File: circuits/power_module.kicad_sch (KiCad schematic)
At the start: 0 parts

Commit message: added 5V reg circuit
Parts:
- added C1: 10uF, symbol Device:C_Small
- added C2, C3: 0.1uF, symbol Device:C_Small
- added C4, C5: 22uF, symbol Device:C_Small
- added C6: 75pF, symbol Device:C_Small
- added J1: Conn_01x02_Pin, symbol Connector:Conn_01x02_Pin
- added L1: 15uH, symbol Device:L_Small
- added R1: 511k, symbol Device:R_Small
- added R2: 105k, symbol Device:R_Small
- added R3: 49.9, symbol Device:R_Small
- added R4: 100k, symbol Device:R_Small
- added R5: 13.3k, symbol Device:R_Small
- added U1: TPS54202DDC, Package_TO_SOT_SMD:SOT-23-6, symbol Regulator_Switching:TPS54202DDC
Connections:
- new net: R1.2, R2.1, U1.5 (EN)
- new net: C6.2, R4.2, R5.1, U1.4 (FB)
- new net: C6.1, R3.2, R4.1
- new net: C3.1, U1.6 (BOOT)
- new net: C3.2, L1.1, U1.2 (SW)
- new net +5V: C4.1, C5.1, L1.2, R3.1
- new net +BATT: C1.1, C2.1, J1.1 (Pin_1), R1.1, U1.3 (VIN)
- new net GND: C1.2, C2.2, C4.2, C5.2, J1.2 (Pin_2), R2.2, R5.2, U1.1 (GND)
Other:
- note added: "5V regulator"

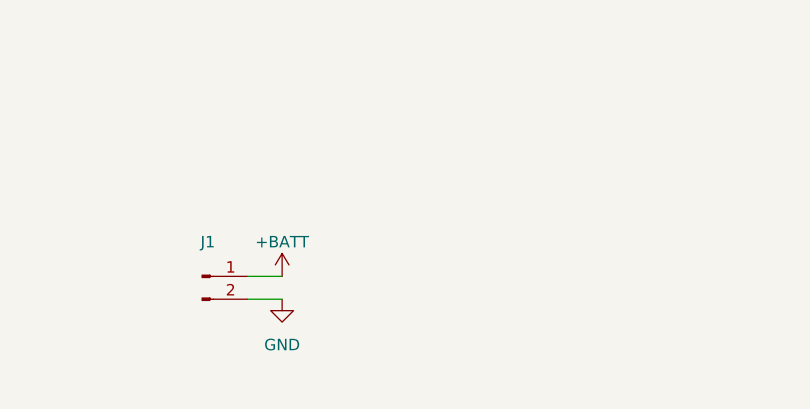
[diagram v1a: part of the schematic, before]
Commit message: motor shield circuit
BTN7030-1EPA
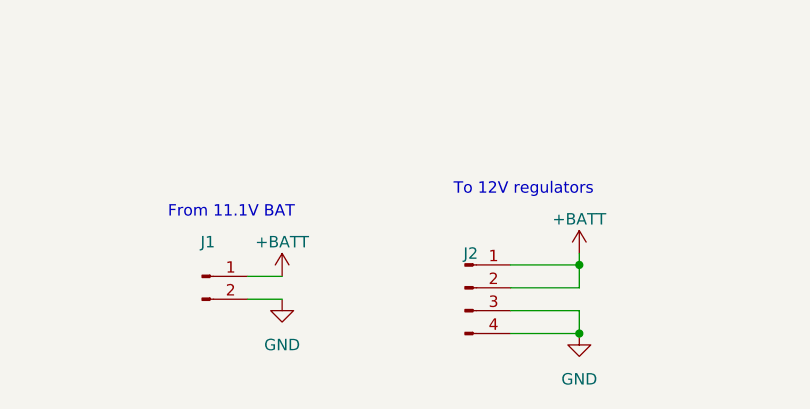
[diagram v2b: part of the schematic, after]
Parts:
- added J2: Conn_01x04_Pin, symbol Connector:Conn_01x04_Pin
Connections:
- net +BATT: now also J2.1 (Pin_1), J2.2 (Pin_2)
- net GND: now also J2.3 (Pin_3), J2.4 (Pin_4)
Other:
- note added: "From 11.1V BAT"
- note added: "To 12V regulators"
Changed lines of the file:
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@@
   (junction (at 105.41 62.23) (diameter 0) (color 0 0 0 0)
   )
+  (junction (at 101.6 185.42) (diameter 0) (color 0 0 0 0)
+  )
   (junction (at 44.45 53.34) (diameter 0) (color 0 0 0 0)
   )
@@
   (junction (at 105.41 55.88) (diameter 0) (color 0 0 0 0)
   )
+  (junction (at 101.6 177.8) (diameter 0) (color 0 0 0 0)
+  )
   (junction (at 119.38 71.12) (diameter 0) (color 0 0 0 0)
   )
@@
     (stroke (width 0) (type default))
   )
+  (wire (pts (xy 93.98 177.8) (xy 101.6 177.8))
+    (stroke (width 0) (type default))
+  )
   (wire (pts (xy 54.61 58.42) (xy 54.61 59.69))
     (stroke (width 0) (type default))
@@
     (stroke (width 0) (type default))
   )
+  (wire (pts (xy 93.98 185.42) (xy 101.6 185.42))
+    (stroke (width 0) (type default))
+  )
   (wire (pts (xy 38.1 50.8) (xy 38.1 53.34))
     (stroke (width 0) (type default))
@@
     (stroke (width 0) (type default))
   )
+  (wire (pts (xy 101.6 182.88) (xy 101.6 185.42))
+    (stroke (width 0) (type default))
+  )
   (wire (pts (xy 124.46 71.12) (xy 124.46 72.39))
     (stroke (width 0) (type default))
@@
     (stroke (width 0) (type default))
   )
+  (wire (pts (xy 93.98 180.34) (xy 101.6 180.34))
+    (stroke (width 0) (type default))
+  )
   (wire (pts (xy 38.1 58.42) (xy 38.1 62.23))
     (stroke (width 0) (type default))
@@
     (stroke (width 0) (type default))
   )
+  (wire (pts (xy 93.98 182.88) (xy 101.6 182.88))
+    (stroke (width 0) (type default))
+  )
+  (wire (pts (xy 101.6 176.53) (xy 101.6 177.8))
+    (stroke (width 0) (type default))
+  )
   (wire (pts (xy 64.77 179.07) (xy 68.58 179.07))
     (stroke (width 0) (type default))
   )
+  (wire (pts (xy 101.6 180.34) (xy 101.6 177.8))
+    (stroke (width 0) (type default))
+  )
   (wire (pts (xy 64.77 181.61) (xy 68.58 181.61))
     (stroke (width 0) (type default))
+  )
+  (text "To 12V regulators" (at 87.63 170.18 0)
+    (effects (font (size 1.27 1.27)) (justify left bottom))
+  )
+  (text "From 11.1V BAT" (at 55.88 172.72 0)
+    (effects (font (size 1.27 1.27)) (justify left bottom))
   )
   (text "5V regulator" (at 27.94 40.64 0)
@@
         (path "/1df96114-eb1a-4ddf-9ea3-acd2b4d12bf3/6683f276-27a3-494e-84c3-353277da8be6"
           (reference "#PWR02") (unit 1)
+        )
+      )
+    )
+  )
+  (symbol (lib_id "power:+BATT") (at 101.6 176.53 0) (unit 1)
+    (in_bom yes) (on_board yes) (dnp no) (fields_autoplaced)
+    (property "Reference" "#PWR09" (at 101.6 180.34 0)
+      (effects (font (size 1.27 1.27)) hide)
+    )
+    (property "Value" "+BATT" (at 101.6 172.72 0)
+      (effects (font (size 1.27 1.27)))
+    )
+    (property "Footprint" "" (at 101.6 176.53 0)
+      (effects (font (size 1.27 1.27)) hide)
+    )
+    (property "Datasheet" "" (at 101.6 176.53 0)
+      (effects (font (size 1.27 1.27)) hide)
+    )
+    (pin "1")
+    (instances
+      (project "rbc_circuits"
+        (path "/1df96114-eb1a-4ddf-9ea3-acd2b4d12bf3/6683f276-27a3-494e-84c3-353277da8be6"
+          (reference "#PWR09") (unit 1)
         )
       )
@@
         )
       )
+    )
+  )
+  (symbol (lib_id "Connector:Conn_01x04_Pin") (at 88.9 180.34 0) (unit 1)
+    (in_bom yes) (on_board yes) (dnp no) (fields_autoplaced)
+    (property "Reference" "J2" (at 89.535 176.53 0)
+      (effects (font (size 1.27 1.27)))
+    )
+    (property "Value" "Conn_01x04_Pin" (at 89.535 176.53 0)
+      (effects (font (size 1.27 1.27)) hide)
+    )
+    (property "Footprint" "" (at 88.9 180.34 0)
+      (effects (font (size 1.27 1.27)) hide)
+    )
+    (property "Datasheet" "~" (at 88.9 180.34 0)
+      (effects (font (size 1.27 1.27)) hide)
+    )
+    (pin "1")
+    (pin "2")
+    (pin "3")
+    (pin "4")
+    (instances
+      (project "rbc_circuits"
+        (path "/1df96114-eb1a-4ddf-9ea3-acd2b4d12bf3/6683f276-27a3-494e-84c3-353277da8be6"
+          (reference "J2") (unit 1)
+        )
+      )
+    )
+  )
+  (symbol (lib_id "power:GND") (at 101.6 185.42 0) (unit 1)
+    (in_bom yes) (on_board yes) (dnp no) (fields_autoplaced)
+    (property "Reference" "#PWR010" (at 101.6 191.77 0)
+      (effects (font (size 1.27 1.27)) hide)
+    )
+    (property "Value" "GND" (at 101.6 190.5 0)
+      (effects (font (size 1.27 1.27)))
+    )
+    (property "Footprint" "" (at 101.6 185.42 0)
+      (effects (font (size 1.27 1.27)) hide)
+    )
+    (property "Datasheet" "" (at 101.6 185.42 0)
+      (effects (font (size 1.27 1.27)) hide)
+    )
+    (pin "1")
+    (instances
+      (project "rbc_circuits"
+        (path "/1df96114-eb1a-4ddf-9ea3-acd2b4d12bf3/6683f276-27a3-494e-84c3-353277da8be6"
+          (reference "#PWR010") (unit 1)
+        )
+      )

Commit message: controller pcb rev 1
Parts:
- removed J2: Conn_01x04_Pin, symbol Connector:Conn_01x04_Pin
- removed R2: 105k, symbol Device:R_Small
- added J2: Conn_01x02_Pin, Connector_PinHeader_2.54mm:PinHeader_1x02_P2.54mm_Vertical, symbol Connector:Conn_01x02_Pin
- added JP1: SolderJumper_2_Open, Jumper:SolderJumper-2_P1.3mm_Open_RoundedPad1.0x1.5mm, symbol Jumper:SolderJumper_2_Open
- added JP2: D3087-98, SamacSys_Parts:D308798, symbol SamacSys_Parts:D3087-98
- C1, C4, C5: footprint (none) -> Capacitor_SMD:C_1206_3216Metric_Pad1.33x1.80mm_HandSolder
- C2, C3: footprint (none) -> Capacitor_SMD:C_0603_1608Metric_Pad1.08x0.95mm_HandSolder
- C6: footprint (none) -> Capacitor_SMD:C_0805_2012Metric_Pad1.18x1.45mm_HandSolder
- J1: footprint (none) -> TerminalBlock_Phoenix:TerminalBlock_Phoenix_MKDS-3-2-5.08_1x02_P5.08mm_Horizontal
- L1: footprint (none) -> LQH3NPH150MMEL:IND_LQH3NPH150MMEL
- R1: value 511k -> 510k; footprint (none) -> Resistor_SMD:R_0805_2012Metric_Pad1.20x1.40mm_HandSolder
- R2: renamed from R3; footprint (none) -> Resistor_SMD:R_0805_2012Metric_Pad1.20x1.40mm_HandSolder
- R3: renamed from R4; footprint (none) -> Resistor_SMD:R_1206_3216Metric_Pad1.30x1.75mm_HandSolder
- R4: renamed from R5; footprint (none) -> Resistor_SMD:R_0805_2012Metric_Pad1.20x1.40mm_HandSolder
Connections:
- net +5V: now also J2.1 (Pin_1)
- net +BATT: now also JP2.2; no longer J1.1 (Pin_1)
- net GND: now also J2.2 (Pin_2)
- net at R1.2: now also JP1.1 (A); no longer U1.5 (EN)
- new net: JP1.2 (B), U1.5 (EN)
- new net: J1.1 (Pin_1), JP2.1
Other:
- note removed: "To 12V regulators"
- moved on the sheet: R1

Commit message: PCB Rev2.0 publish
It's here
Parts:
- removed C2: 0.1uF, Capacitor_SMD:C_0603_1608Metric_Pad1.08x0.95mm_HandSolder, symbol Device:C_Small
- removed J2: Conn_01x02_Pin, Connector_PinHeader_2.54mm:PinHeader_1x02_P2.54mm_Vertical, symbol Connector:Conn_01x02_Pin
- removed JP1: SolderJumper_2_Open, Jumper:SolderJumper-2_P1.3mm_Open_RoundedPad1.0x1.5mm, symbol Jumper:SolderJumper_2_Open
- removed JP2: D3087-98, SamacSys_Parts:D308798, symbol SamacSys_Parts:D3087-98
- removed U1: TPS54202DDC, Package_TO_SOT_SMD:SOT-23-6, symbol Regulator_Switching:TPS54202DDC
- added C10, C17, C18: 100uF, SamacSys_Parts:16SVF180M, symbol Device:C_Polarized_Small
- added C11, C12, C2: 270uF, SamacSys_Parts:EEHZS1H221P, symbol Device:C_Polarized_Small
- added C13, C14: 100nF, Capacitor_SMD:C_0402_1005Metric, symbol Device:C_Small
- added C15, C16, C8: 10nF, Capacitor_SMD:C_0805_2012Metric, symbol Device:C_Small
- added C7: 10pF, Capacitor_SMD:C_0603_1608Metric, symbol Device:C_Small
- added C9: 22uF, Capacitor_SMD:C_1206_3216Metric, symbol Device:C_Small
- added D1, D2, D3: 450mV 3A, Diode_SMD:D_SMA, symbol Device:D_Schottky_Small
- added IC1: LT8609AEDDM#PBF, SamacSys_Parts:SON50P300X300X80-11N-D, symbol SamacSys_Parts:LT8609AEDDM#PBF
- added IC2, IC3, IC4: LM2678SX-ADJ/NOPB, rbc Custom Library:KTW0007B_custom, symbol SamacSys_Parts:LM2678SX-5.0_NOPB
- added J?: Extra, Connector_PinHeader_2.54mm:PinHeader_2x02_P2.54mm_Vertical, symbol Connector:Conn_01x04_Pin
- added JP1: EN, Jumper:SolderJumper-3_P2.0mm_Open_TrianglePad1.0x1.5mm, symbol Jumper:SolderJumper_3_Open
- added L2, L3, L4: 22uH, SamacSys_Parts:INDPM110100X400N, symbol Device:L_Small
- added R10, R9: 8.87k, Resistor_SMD:R_0603_1608Metric, symbol Device:R_Small
- added R5: 1M, Resistor_SMD:R_0402_1005Metric, symbol Device:R_Small
- added R6: 100k, Resistor_SMD:R_0201_0603Metric, symbol Device:R_Small
- added R7, R8: 1k, Resistor_SMD:R_0201_0603Metric, symbol Device:R_Small
- C1: value 10uF -> 1uF; footprint Capacitor_SMD:C_1206_3216Metric_Pad1.33x1.80mm_HandSolder -> Capacitor_SMD:C_0603_1608Metric; Part No. (none) -> TCC0603X5R105K250CT
- C3: value 0.1uF -> 4.7uF; footprint Capacitor_SMD:C_0603_1608Metric_Pad1.08x0.95mm_HandSolder -> Capacitor_SMD:C_1206_3216Metric; Part No. (none) -> CGA5L1X7R1H475KT0Y0S
- C4: value 22uF -> 10nF; footprint Capacitor_SMD:C_1206_3216Metric_Pad1.33x1.80mm_HandSolder -> Capacitor_SMD:C_0402_1005Metric; Part No. (none) -> HGC0402R7103K500NTEJ
- C5: value 22uF -> 100nF; footprint Capacitor_SMD:C_1206_3216Metric_Pad1.33x1.80mm_HandSolder -> Capacitor_SMD:C_0402_1005Metric
- C6: value 75pF -> 100nF; footprint Capacitor_SMD:C_0805_2012Metric_Pad1.18x1.45mm_HandSolder -> Capacitor_SMD:C_0402_1005Metric; Part No. (none) -> GRM155R71H104KE14J
- L1: value 15uH -> 2.2uH; footprint LQH3NPH150MMEL:IND_LQH3NPH150MMEL -> SamacSys_Parts:INDC4441X200N; Part No. (none) -> SRP4020TA-2R2M
- R1: value 510k -> 18.2k; footprint Resistor_SMD:R_0805_2012Metric_Pad1.20x1.40mm_HandSolder -> Resistor_SMD:R_0603_1608Metric_Pad0.98x0.95mm_HandSolder; Part No. (none) -> CRCW060318K2FKEA
- R2: value 49.9 -> 1k; footprint Resistor_SMD:R_0805_2012Metric_Pad1.20x1.40mm_HandSolder -> Resistor_SMD:R_0201_0603Metric; Part No. (none) -> RC0201FR-071KL
- R3: value 100k -> 187k; footprint Resistor_SMD:R_1206_3216Metric_Pad1.30x1.75mm_HandSolder -> Resistor_SMD:R_0603_1608Metric; Part No. (none) -> AC0603FR-07187KL
- R4: value 13.3k -> 8.87k; footprint Resistor_SMD:R_0805_2012Metric_Pad1.20x1.40mm_HandSolder -> Resistor_SMD:R_0603_1608Metric; Part No. (none) -> RT0603BRE078K87L
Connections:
- net +5V: now also J?.1 (Pin_1), J?.2 (Pin_2), JP1.1 (A), JP1.3 (B); no longer C4.1, C5.1, L1.2, R2.1
- net +BATT: now also C3.2, C5.2, J1.1 (Pin_1), C11.1, C12.1, C13.2, C14.2, C2.1, IC1.10 (EN/UV), IC1.9 (VIN), IC2.2 (INPUT), IC3.2 (INPUT), IC4.2 (INPUT); no longer C1.1, R1.1
- net GND: now also C1.1, C3.1, C4.1, C5.1, R1.2, R2.2, R3.2, C10.2, C11.2, C12.2, C13.1, C14.1, C17.2, C18.2, C2.2, C9.1, D1.2 (A), D2.2 (A), D3.2 (A), IC1.11 (GND), IC2.4 (GND), IC3.4 (GND), IC4.4 (GND), J?.3 (Pin_3), J?.4 (Pin_4), R7.2, R8.2; no longer C1.2, C4.2, C5.2, R4.2
- net at L1.1: now also C6.2, IC1.2 (SW); no longer C3.2
- new net: C16.1, D3.1 (K), IC4.1 (SWITCH_OUTPUT), L4.1
- new net: C16.2, IC4.3 (CB)
- new net: IC4.6 (FB), R10.2, R8.1
- new net: IC2.6 (FB), R2.1, R4.2
- new net: IC1.4 (RT), R1.1
- new net: C7.2, C9.2, JP1.2 (C), L1.2, R5.1, R6.1
- new net: C15.1, D2.1 (K), IC3.1 (SWITCH_OUTPUT), L3.1
- new net: C8.1, D1.1 (K), IC2.1 (SWITCH_OUTPUT), L2.1
- new net: C8.2, IC2.3 (CB)
- new net: C15.2, IC3.3 (CB)
- new net: C6.1, IC1.1 (BST)
- new net: IC1.8 (PG), R6.2
- new net: C1.2, IC1.3 (INTVCC), IC1.5 (SYNC)
- new net: C7.1, IC1.6 (FB), R3.1, R5.2
- new net: C4.2, IC1.7 (TR/SS)
- new net: IC3.6 (FB), R7.1, R9.2
- new net +12C: C10.1, L2.2, R4.1
- new net +12P: C18.1, L4.2, R10.1
- new net +12V: C17.1, L3.2, R9.1
- no-connect marks 0 -> 6
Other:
- note added: "16SVPC100M"
- note added: "B340LA-13-F"
- note added: "CL21C103JBFNNNE"
- note added: "From 6S BAT"
- note added: "M1 12V regulator"
- note added: "M2 12V regulator"
- note added: "M3 12V regulator"
- note added: "make sure L can handle >3A"
- note removed: "From 11.1V BAT"
- title: (none) -> RBC by UGS
